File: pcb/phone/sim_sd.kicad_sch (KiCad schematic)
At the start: 7 parts, among them U10 ESDA6V1-5SC6, U11 ESDA6V1-5SC6

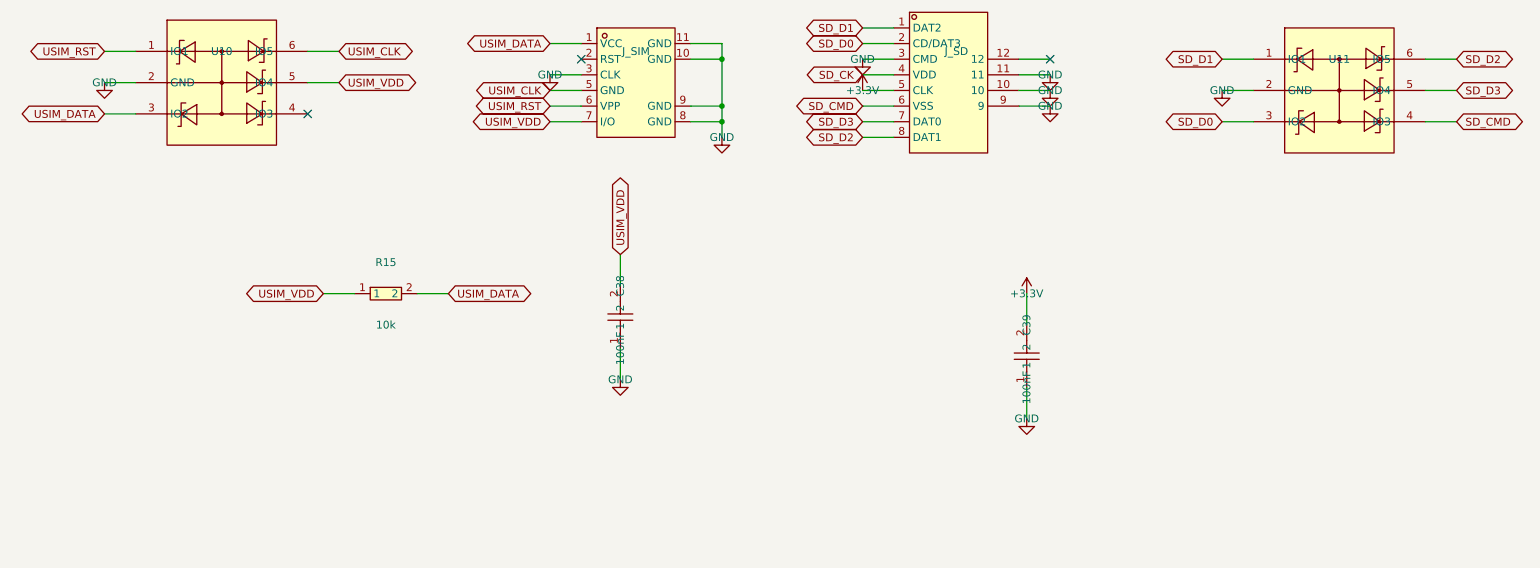
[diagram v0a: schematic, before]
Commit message: Cleanup: remove rejected part symbols, one-off scripts, stale datasheets
- Remove 7 rejected symbols from easyeda2kicad.kicad_sym (PJ-327C-4A,
  PJ-3250-5A, PJ-3240-5A, TYPE-C16PLC-H10.0, PJ-327A5JJ, PJ-327-P5,
  TYPEC-306DDW-ARP16) — replaced by Tensility 54-00298 and GCT USB4085-GF-A
- Delete 10 one-off inspection scripts (check_*.py, find_*.py, dump_*.py,
  extract_*.py) — keep only gen_*.py schematic generators
- Delete rejected datasheets (pj3126-5a, pj3240-5a, pj3250-5a, pj3f07-5p,
  N114 superseded display)
- Delete generated BOM/POS CSV files
- Add alps-ssss2.pdf and gct-usb4085.pdf to reference README index
- Include all schematic changes from previous sessions (SD pullups, VBUS
  divider fix, level shifter verification, codec caps, DCVDD fix)

Generated with [Devin](https://devin.ai)

Co-Authored-By: Devin <158243242+devin-ai-integration[bot]@users.noreply.github.com>
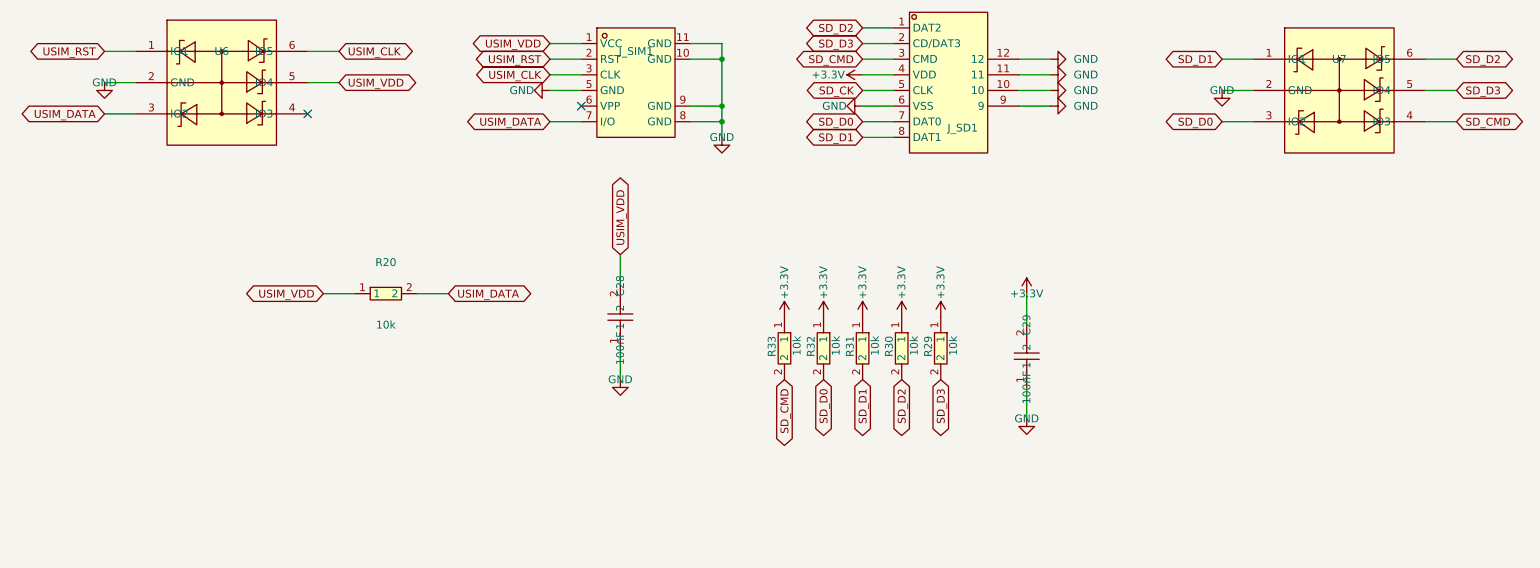
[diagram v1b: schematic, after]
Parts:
- added R29, R30, R31, R32, R33: 10k, easyeda2kicad:R0603, symbol passives:RC0603JR-0710KL
- renumbered C38 to C28, C39 to C29, J_SD to J_SD1, J_SIM to J_SIM1, R15 to R20, U10 to U6, U11 to U7
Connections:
- net +3.3V: now also J_SD1.4 (VDD), R29.1, R30.1, R31.1, R32.1, R33.1; no longer J_SD1.5 (CLK)
- net GND: now also J_SD1.12, J_SD1.6 (VSS), J_SIM1.5 (GND); no longer J_SD1.3 (CMD), J_SIM1.3 (CLK)
- net SD_CK: now also J_SD1.5 (CLK); no longer J_SD1.4 (VDD)
- net SD_CMD: now also J_SD1.3 (CMD), R33.2; no longer J_SD1.6 (VSS)
- net SD_D0: now also J_SD1.7 (DAT0), R32.2; no longer J_SD1.2 (CD/DAT3)
- net SD_D1: now also J_SD1.8 (DAT1), R31.2; no longer J_SD1.1 (DAT2)
- net SD_D2: now also J_SD1.1 (DAT2), R30.2; no longer J_SD1.8 (DAT1)
- net SD_D3: now also J_SD1.2 (CD/DAT3), R29.2; no longer J_SD1.7 (DAT0)
- net USIM_CLK: now also J_SIM1.3 (CLK); no longer J_SIM1.5 (GND)
- net USIM_DATA: now also J_SIM1.7 (I/O); no longer J_SIM1.1 (VCC)
- net USIM_RST: now also J_SIM1.2 (RST); no longer J_SIM1.6 (VPP)
- net USIM_VDD: now also J_SIM1.1 (VCC); no longer J_SIM1.7 (I/O)
- no-connect marks 3 -> 2

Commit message: Restructure display sheet for candybar + fix pinout + add backlight FET + power switch reversal
Display sheet (LOCKED):
- Fix J_DISP1 pinout to match HS20HS072RX datasheet (was 1/12 correct, now all 14 pins match)
- Add backlight FET circuit: Q1 (AO3400A), R20 (100ohm gate), R5 (10k pulldown), R19 moved to pin 10
- Fix R19 MPN: was 470ohm part with 4.7ohm value, swapped to RC0603JR-074R7L (correct 4.7ohm)
- Move display power from +1V8 to +3.3V (1.8V below VCC min 2.4V)
- Remove display_daughter sheet entry, J_HINGE1, J_HINGE2, OUTER_CS/OUTER_DC
- Add no-connect flags on MCU PG9/PG10 (freed from outer display)
- FPC connector orientation review flagged for PCB layout phase

Power switch (reversed 2026-08-27):
- Move SW21 from battery path back to TPS63021 EN pin (signal-level)
- Select C&K OS102011MA1QN1 (100mA SPDT, LCSC C226259), 8.4mm actuator, usable as finger toggle
- Battery always connected, charging while off restored
- Supersedes 2026-08-17 battery-path architecture

New library parts:
- ics:AO3400A (N-ch MOSFET, SOT-23, LCSC C20917)
- passives:0603WAF1000T5E (100ohm 0603, LCSC C22775)
- passives:RC0603JR-074R7L (4.7ohm 0603, LCSC C137621)
- electromech:OS102011MA1QN1 (SPDT slide switch, LCSC C226259)

Docs updated:
- project-log: 3 new entries (display review, power switch reversal, USB hub)
- bom.md: item 25b switch selected, display backlight parts
- block-diagram.md: +BATT net (no switch), U8 EN pin (switched by SW21)
- schematic-completion-plan.md: display sheet LOCKED, section F complete
- task-tracker.md: O2 updated with 2026-08-27 architecture
- ic-by-ic-review.md: Q3 superseded again, DEF-001 updated
- datasheets/README.md: HS20HS072RX pinout verified, SPI confirmed

Generated with [Devin](https://devin.ai)

Co-Authored-By: Devin <158243242+devin-ai-integration[bot]@users.noreply.github.com>
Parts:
- removed R20: 10k, easyeda2kicad:R0603, symbol passives:RC0603JR-0710KL
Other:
- note added: "LOCKED 8/29 MD"
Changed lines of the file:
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@@
 		(title "SIM_SD")
 	)
+	(text "LOCKED 8/29 MD"
+		(exclude_from_sim no)
+		(at 180.34 170.942 0)
+		(effects
+			(font
+				(size 1.27 1.27)
+			)
+		)
+	)
 	(junction
 		(at 149.86 101.6)
@@
 	(wire
 		(pts
-			(xy 90.17 129.54) (xy 85.09 129.54)
-		)
-		(stroke
-			(width 0)
-			(type default)
-		)
-	)
-	(wire
-		(pts
 			(xy 127 93.98) (xy 121.92 93.98)
 		)
@@
 	(wire
 		(pts
-			(xy 100.33 129.54) (xy 105.41 129.54)
-		)
-		(stroke
-			(width 0)
-			(type default)
-		)
-	)
-	(wire
-		(pts
 			(xy 177.8 104.14) (xy 172.72 104.14)
 		)
@@
 		)
 	)
-	(global_label "USIM_DATA"
-		(shape bidirectional)
-		(at 105.41 129.54 0)
-		(fields_autoplaced yes)
-		(effects
-			(font
-				(size 1.27 1.27)
-			)
-			(justify left)
-		)
-		(property "Intersheetrefs" "${INTERSHEET_REFS}"
-			(at 105.41 129.54 0)
-			(hide yes)
-			(show_name no)
-			(do_not_autoplace no)
-			(effects
-				(font
-					(size 1.27 1.27)
-				)
-				(justify left)
-			)
-		)
-	)
 	(global_label "SD_D2"
 		(shape bidirectional)
@@
 		)
 	)
-	(global_label "USIM_VDD"
-		(shape bidirectional)
-		(at 85.09 129.54 180)
-		(fields_autoplaced yes)
-		(effects
-			(font
-				(size 1.27 1.27)
-			)
-			(justify right)
-		)
-		(property "Intersheetrefs" "${INTERSHEET_REFS}"
-			(at 85.09 129.54 0)
-			(hide yes)
-			(show_name no)
-			(do_not_autoplace no)
-			(effects
-				(font
-					(size 1.27 1.27)
-				)
-				(justify right)
-			)
-		)
-	)
 	(global_label "SD_CMD"
 		(shape bidirectional)
@@
 					(unit 1)
 				)
-			)
-		)
-	)
-	(symbol
-		(lib_id "passives:RC0603JR-0710KL")
-		(at 95.25 129.54 0)
-		(unit 1)
-		(body_style 1)
-		(exclude_from_sim no)
-		(in_bom yes)
-		(on_board yes)
-		(in_pos_files yes)
-		(dnp no)
-		(fields_autoplaced yes)
-		(property "Reference" "R20"
-			(at 95.25 124.46 0)
-			(show_name no)
-			(do_not_autoplace no)
-			(effects
-				(font
-					(size 1.27 1.27)
-				)
-			)
-		)
-		(property "Value" "10k"
-			(at 95.25 134.62 0)
-			(show_name no)
-			(do_not_autoplace no)
-			(effects
-				(font
-					(size 1.27 1.27)
-				)
-			)
-		)
-		(property "Footprint" "easyeda2kicad:R0603"
-			(at 95.25 129.54 0)
-			(hide yes)
-			(show_name no)
-			(do_not_autoplace no)
-			(effects
-				(font
-					(size 1.27 1.27)
-				)
-			)
-		)
-		(property "Datasheet" ""
-			(at 95.25 129.54 0)
-			(hide yes)
-			(show_name no)
-			(do_not_autoplace no)
-			(effects
-				(font
-					(size 1.27 1.27)
-				)
-			)
-		)
-		(property "Description" "10k SIM data pull-up resistor"
-			(at 95.25 129.54 0)
-			(hide yes)
-			(show_name no)
-			(do_not_autoplace no)
-			(effects
-				(font
-					(size 1.27 1.27)
-				)
-			)
-		)
-		(pin "1"
-		)
-		(pin "2"
-		)
-		(instances
-			(project "phone"
-				(path "/451c3b43-1616-42cb-bf96-d436f4db82c2/7fc639d9-249c-4f41-85eb-7c2617f3c206"
-					(reference "R20")
-					(unit 1)
-				)
